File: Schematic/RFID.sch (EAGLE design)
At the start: 24 parts, among them IC1 B82450A1084C000, Q8 125kHz, U1 HTRC11001T/02EE,11

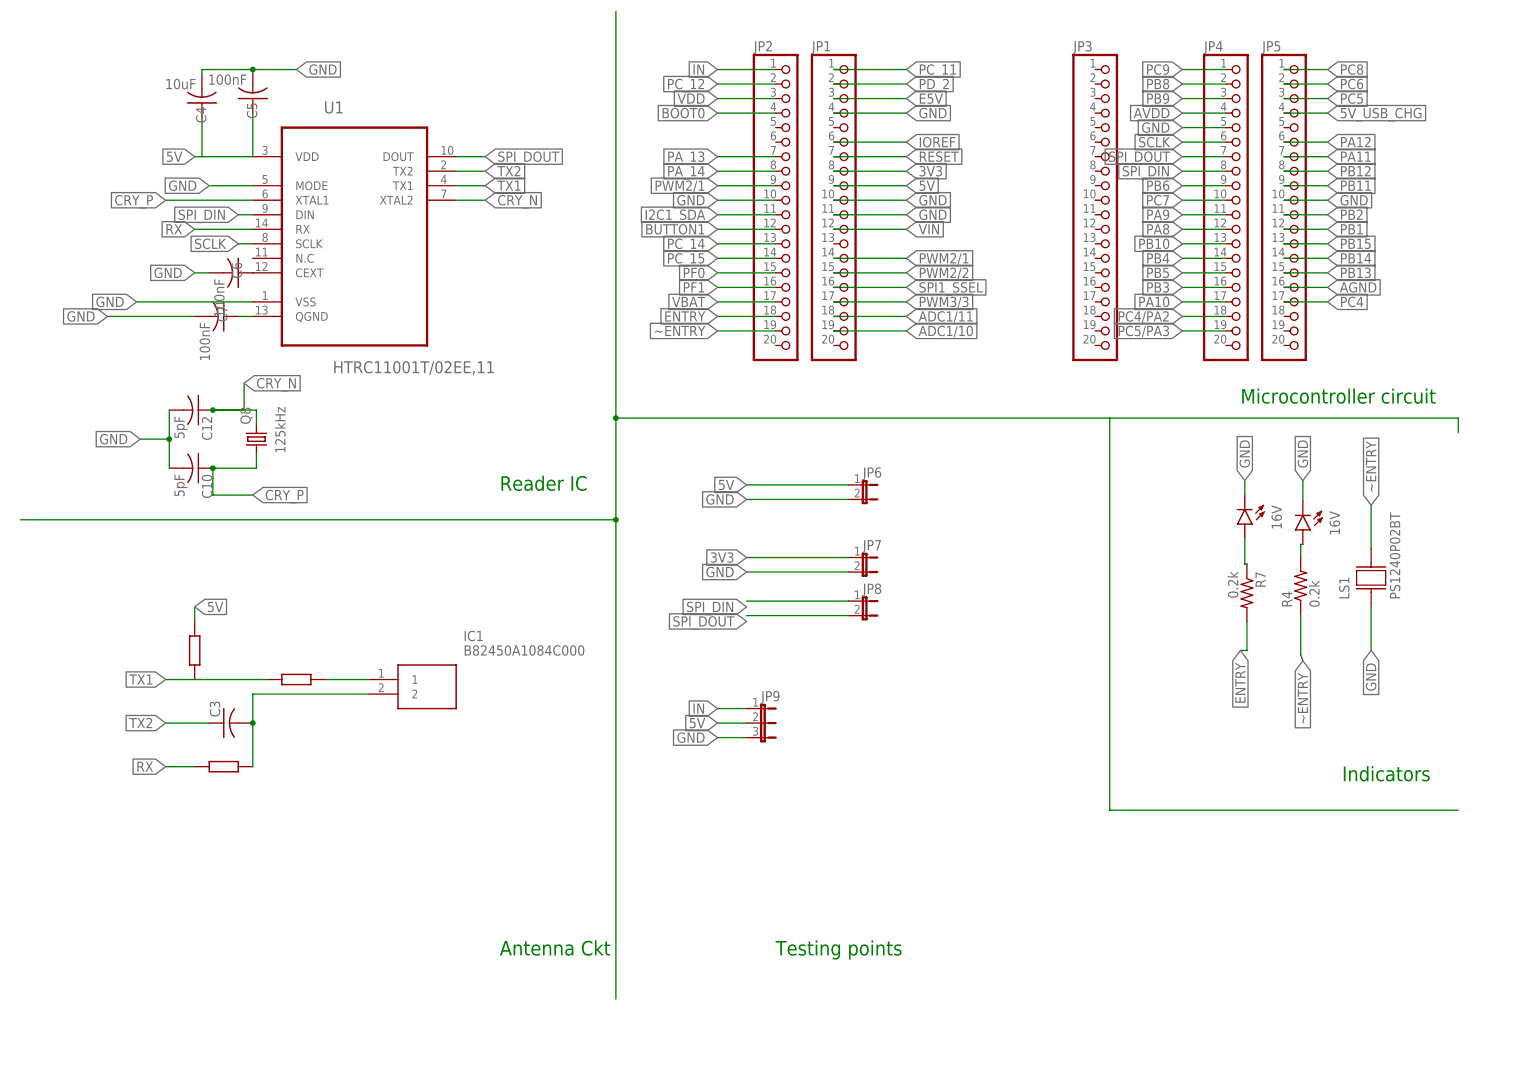
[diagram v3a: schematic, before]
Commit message: Buzzer+impedance matching ckt incorporated
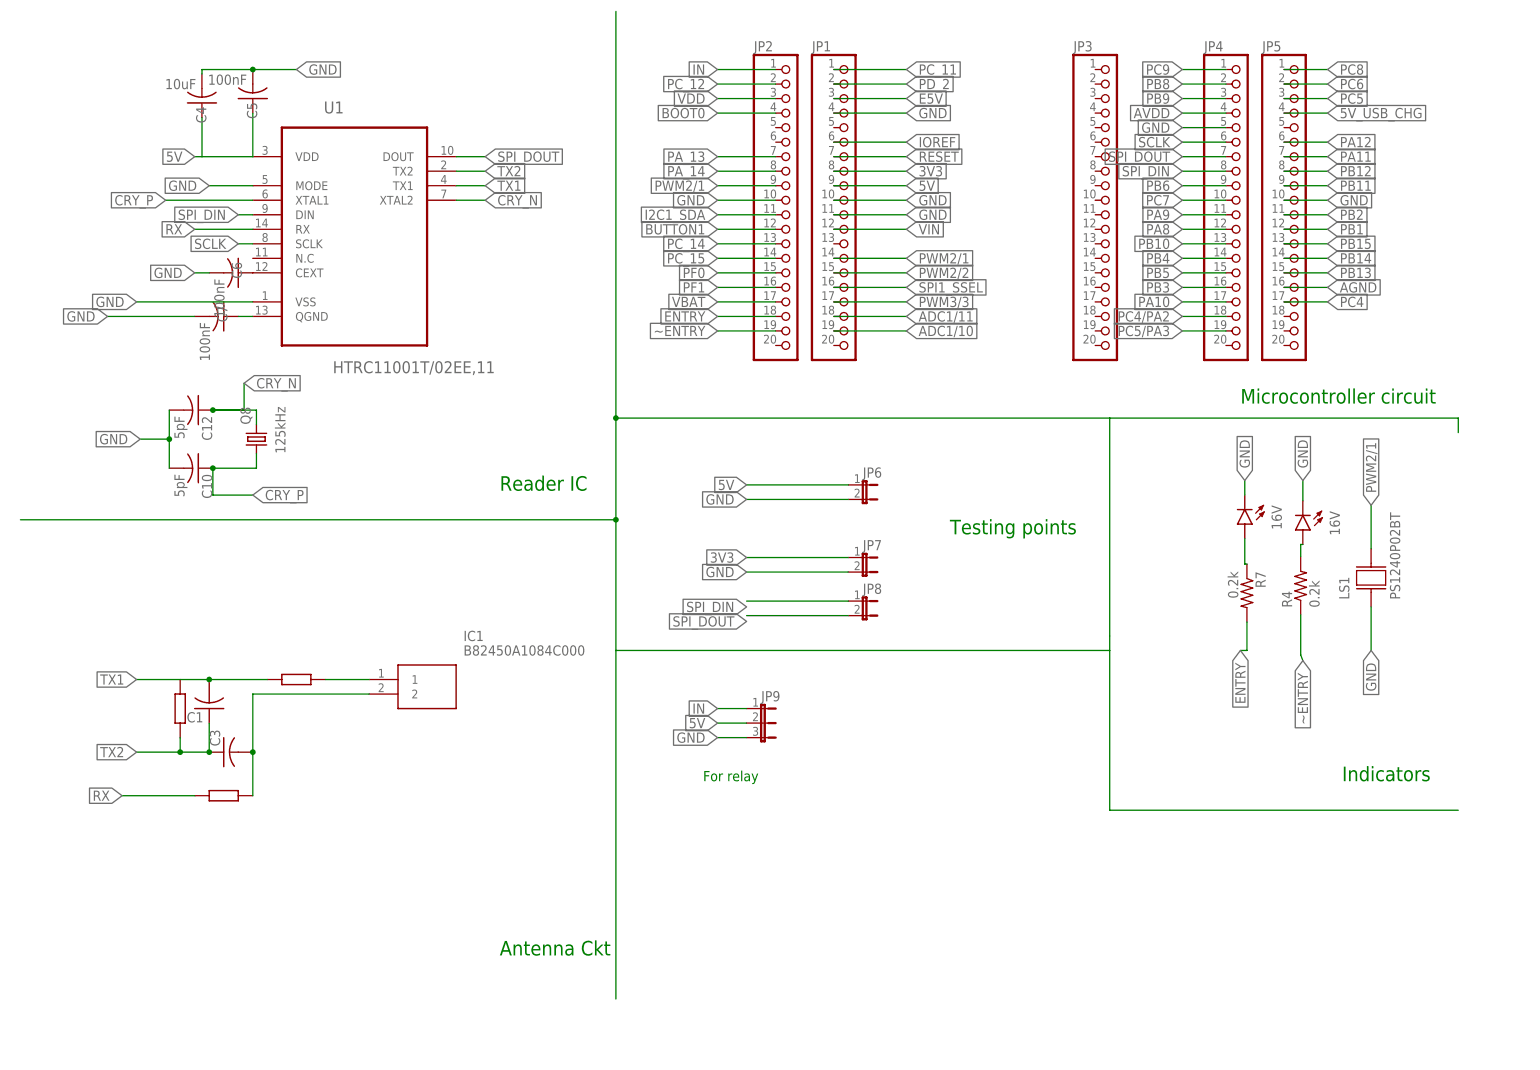
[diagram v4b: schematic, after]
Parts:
- added C1: (no value), rcl:C-USC0805
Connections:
- net PWM2/1: now also LS1.2
- net TX1: now also C1.2
- net TX2: now also C1.1
- net ~ENTRY: no longer LS1.2
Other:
- note added: "For relay"
- moved on the sheet: C3
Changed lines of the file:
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@@
 <part name="IC1" library="B82450A1084C000" deviceset="B82450A1084C000" device=""/>
 <part name="R1" library="docu-dummy" library_urn="urn:adsk.eagle:library:215" deviceset="R" device=""/>
-<part name="R2" library="docu-dummy" library_urn="urn:adsk.eagle:library:215" deviceset="R" device=""/>
 <part name="R3" library="docu-dummy" library_urn="urn:adsk.eagle:library:215" deviceset="R" device=""/>
 <part name="C3" library="rcl" library_urn="urn:adsk.eagle:library:334" deviceset="C-US" device="C0805" package3d_urn="urn:adsk.eagle:package:23617/2"/>
@@
 <part name="LS1" library="PS1240P02BT" deviceset="PS1240P02BT" device=""/>
 <part name="JP9" library="jumper" library_urn="urn:adsk.eagle:library:252" deviceset="JP2E" device="" package3d_urn="urn:adsk.eagle:package:15452/1"/>
+<part name="C1" library="rcl" library_urn="urn:adsk.eagle:library:334" deviceset="C-US" device="C0805" package3d_urn="urn:adsk.eagle:package:23617/2"/>
+<part name="R5" library="docu-dummy" library_urn="urn:adsk.eagle:library:215" deviceset="R" device=""/>
 </parts>
 <sheets>
@@
 <text x="48.26" y="53.34" size="2.54" layer="91">Antenna Ckt</text>
 <text x="177.8" y="149.86" size="2.54" layer="91">Microcontroller circuit</text>
-<text x="96.52" y="53.34" size="2.54" layer="91">Testing points</text>
+<text x="127" y="127" size="2.54" layer="91">Testing points</text>
 <text x="195.58" y="83.82" size="2.54" layer="91">Indicators</text>
+<text x="83.82" y="83.82" size="1.778" layer="91">For relay</text>
 </plain>
 <instances>
@@
 </instance>
 <instance part="R1" gate="G$1" x="12.7" y="101.6" smashed="yes"/>
-<instance part="R2" gate="G$1" x="-5.08" y="106.68" smashed="yes" rot="R90"/>
-<instance part="R3" gate="G$1" x="0" y="86.36" smashed="yes" rot="R180"/>
-<instance part="C3" gate="G$1" x="0" y="93.98" smashed="yes" rot="R90">
-<attribute name="NAME" x="-0.635" y="94.996" size="1.778" layer="95" rot="R90"/>
-<attribute name="VALUE" x="4.191" y="94.996" size="1.778" layer="96" rot="R90"/>
+<instance part="R3" gate="G$1" x="0" y="81.28" smashed="yes" rot="R180"/>
+<instance part="C3" gate="G$1" x="0" y="88.9" smashed="yes" rot="R90">
+<attribute name="NAME" x="-0.635" y="89.916" size="1.778" layer="95" rot="R90"/>
+<attribute name="VALUE" x="4.191" y="89.916" size="1.778" layer="96" rot="R90"/>
 </instance>
 <instance part="C4" gate="G$1" x="-3.81" y="202.438" smashed="yes" rot="R180">
@@
 <attribute name="VALUE" x="93.98" y="88.265" size="1.778" layer="96"/>
 </instance>
+<instance part="C1" gate="G$1" x="-2.54" y="96.52" smashed="yes" rot="R180">
+<attribute name="NAME" x="-3.556" y="95.885" size="1.778" layer="95" rot="R180"/>
+<attribute name="VALUE" x="-3.556" y="100.711" size="1.778" layer="96" rot="R180"/>
+</instance>
+<instance part="R5" gate="G$1" x="-7.62" y="96.52" smashed="yes" rot="R90"/>
 </instances>
 <busses>
@@
 </segment>
 <segment>
-<wire x1="-5.08" y1="111.76" x2="-5.08" y2="114.3" width="0.1524" layer="91"/>
-<label x="-5.08" y="114.3" size="1.778" layer="95" xref="yes"/>
-</segment>
-<segment>
 <label x="91.44" y="135.636" size="1.778" layer="95" rot="R180" xref="yes"/>
 <wire x1="109.22" y1="135.636" x2="91.44" y2="135.636" width="0.1524" layer="91"/>
@@
 <wire x1="106.68" y1="175.26" x2="119.38" y2="175.26" width="0.1524" layer="91"/>
 <label x="119.38" y="175.26" size="1.778" layer="95" xref="yes"/>
+</segment>
+<segment>
+<pinref part="LS1" gate="G$1" pin="2"/>
+<wire x1="200.66" y1="124.46" x2="200.66" y2="132.08" width="0.1524" layer="91"/>
+<label x="200.66" y="132.08" size="1.778" layer="95" rot="R90" xref="yes"/>
 </segment>
 </net>
@@
 <pinref part="IC1" gate="G$1" pin="2"/>
 <pinref part="C3" gate="G$1" pin="2"/>
-<wire x1="5.08" y1="93.98" x2="5.08" y2="99.06" width="0.1524" layer="91"/>
+<wire x1="5.08" y1="88.9" x2="5.08" y2="99.06" width="0.1524" layer="91"/>
 <wire x1="5.08" y1="99.06" x2="25.4" y2="99.06" width="0.1524" layer="91"/>
-<wire x1="5.08" y1="93.98" x2="5.08" y2="86.36" width="0.1524" layer="91"/>
-<junction x="5.08" y="93.98"/>
+<wire x1="5.08" y1="88.9" x2="5.08" y2="81.28" width="0.1524" layer="91"/>
+<junction x="5.08" y="88.9"/>
 </segment>
 </net>
@@
 <segment>
 <pinref part="C3" gate="G$1" pin="1"/>
-<wire x1="-2.54" y1="93.98" x2="-10.16" y2="93.98" width="0.1524" layer="91"/>
-<label x="-10.16" y="93.98" size="1.778" layer="95" rot="R180" xref="yes"/>
+<wire x1="-2.54" y1="88.9" x2="-7.62" y2="88.9" width="0.1524" layer="91"/>
+<label x="-15.24" y="88.9" size="1.778" layer="95" rot="R180" xref="yes"/>
+<pinref part="C1" gate="G$1" pin="1"/>
+<junction x="-2.54" y="88.9"/>
+<wire x1="-7.62" y1="88.9" x2="-15.24" y2="88.9" width="0.1524" layer="91"/>
+<wire x1="-2.54" y1="88.9" x2="-2.54" y2="93.98" width="0.1524" layer="91"/>
+<wire x1="-7.62" y1="91.44" x2="-7.62" y2="88.9" width="0.1524" layer="91"/>
+<junction x="-7.62" y="88.9"/>
 </segment>
 </net>
@@
 </segment>
 <segment>
-<wire x1="7.62" y1="101.6" x2="-10.16" y2="101.6" width="0.1524" layer="91"/>
-<label x="-10.16" y="101.6" size="1.778" layer="95" rot="R180" xref="yes"/>
+<wire x1="7.62" y1="101.6" x2="-2.54" y2="101.6" width="0.1524" layer="91"/>
+<label x="-15.24" y="101.6" size="1.778" layer="95" rot="R180" xref="yes"/>
+<pinref part="C1" gate="G$1" pin="2"/>
+<wire x1="-2.54" y1="101.6" x2="-15.24" y2="101.6" width="0.1524" layer="91"/>
+<junction x="-2.54" y="101.6"/>
 </segment>
 </net>
@@
 </segment>
 <segment>
-<wire x1="-5.08" y1="86.36" x2="-10.16" y2="86.36" width="0.1524" layer="91"/>
-<label x="-10.16" y="86.36" size="1.778" layer="95" rot="R180" xref="yes"/>
+<wire x1="-5.08" y1="81.28" x2="-17.78" y2="81.28" width="0.1524" layer="91"/>
+<label x="-17.78" y="81.28" size="1.778" layer="95" rot="R180" xref="yes"/>
 </segment>
 </net>
@@
 <wire x1="68.58" y1="147.32" x2="68.58" y2="129.54" width="0.1524" layer="91"/>
 <wire x1="68.58" y1="129.54" x2="-35.56" y2="129.54" width="0.1524" layer="91"/>
-<wire x1="68.58" y1="129.54" x2="68.58" y2="45.72" width="0.1524" layer="91"/>
+<wire x1="68.58" y1="129.54" x2="68.58" y2="106.68" width="0.1524" layer="91"/>
 <junction x="68.58" y="129.54"/>
+<wire x1="68.58" y1="106.68" x2="68.58" y2="45.72" width="0.1524" layer="91"/>
 <wire x1="68.58" y1="147.32" x2="154.94" y2="147.32" width="0.1524" layer="91"/>
 <wire x1="154.94" y1="147.32" x2="215.9" y2="147.32" width="0.1524" layer="91"/>
 <wire x1="215.9" y1="147.32" x2="215.9" y2="144.78" width="0.1524" layer="91"/>
 <junction x="68.58" y="147.32"/>
-<wire x1="154.94" y1="147.32" x2="154.94" y2="78.74" width="0.1524" layer="91"/>
+<wire x1="154.94" y1="147.32" x2="154.94" y2="109.22" width="0.1524" layer="91"/>
+<wire x1="154.94" y1="106.68" x2="154.94" y2="78.74" width="0.1524" layer="91"/>
 <wire x1="154.94" y1="78.74" x2="215.9" y2="78.74" width="0.1524" layer="91"/>
+<wire x1="68.58" y1="106.68" x2="154.94" y2="106.68" width="0.1524" layer="91"/>
+<wire x1="154.94" y1="106.68" x2="154.94" y2="109.22" width="0.1524" layer="91"/>
 </segment>
 </net>
@@
 <net name="~ENTRY" class="2">
 <segment>
-<pinref part="LS1" gate="G$1" pin="2"/>
-<wire x1="200.66" y1="124.46" x2="200.66" y2="132.08" width="0.1524" layer="91"/>
-<label x="200.66" y="132.08" size="1.778" layer="95" rot="R90" xref="yes"/>
-</segment>
-<segment>
 <pinref part="R4" gate="G$1" pin="1"/>
